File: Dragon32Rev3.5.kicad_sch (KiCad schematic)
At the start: 8 parts, among them SW1 RESET

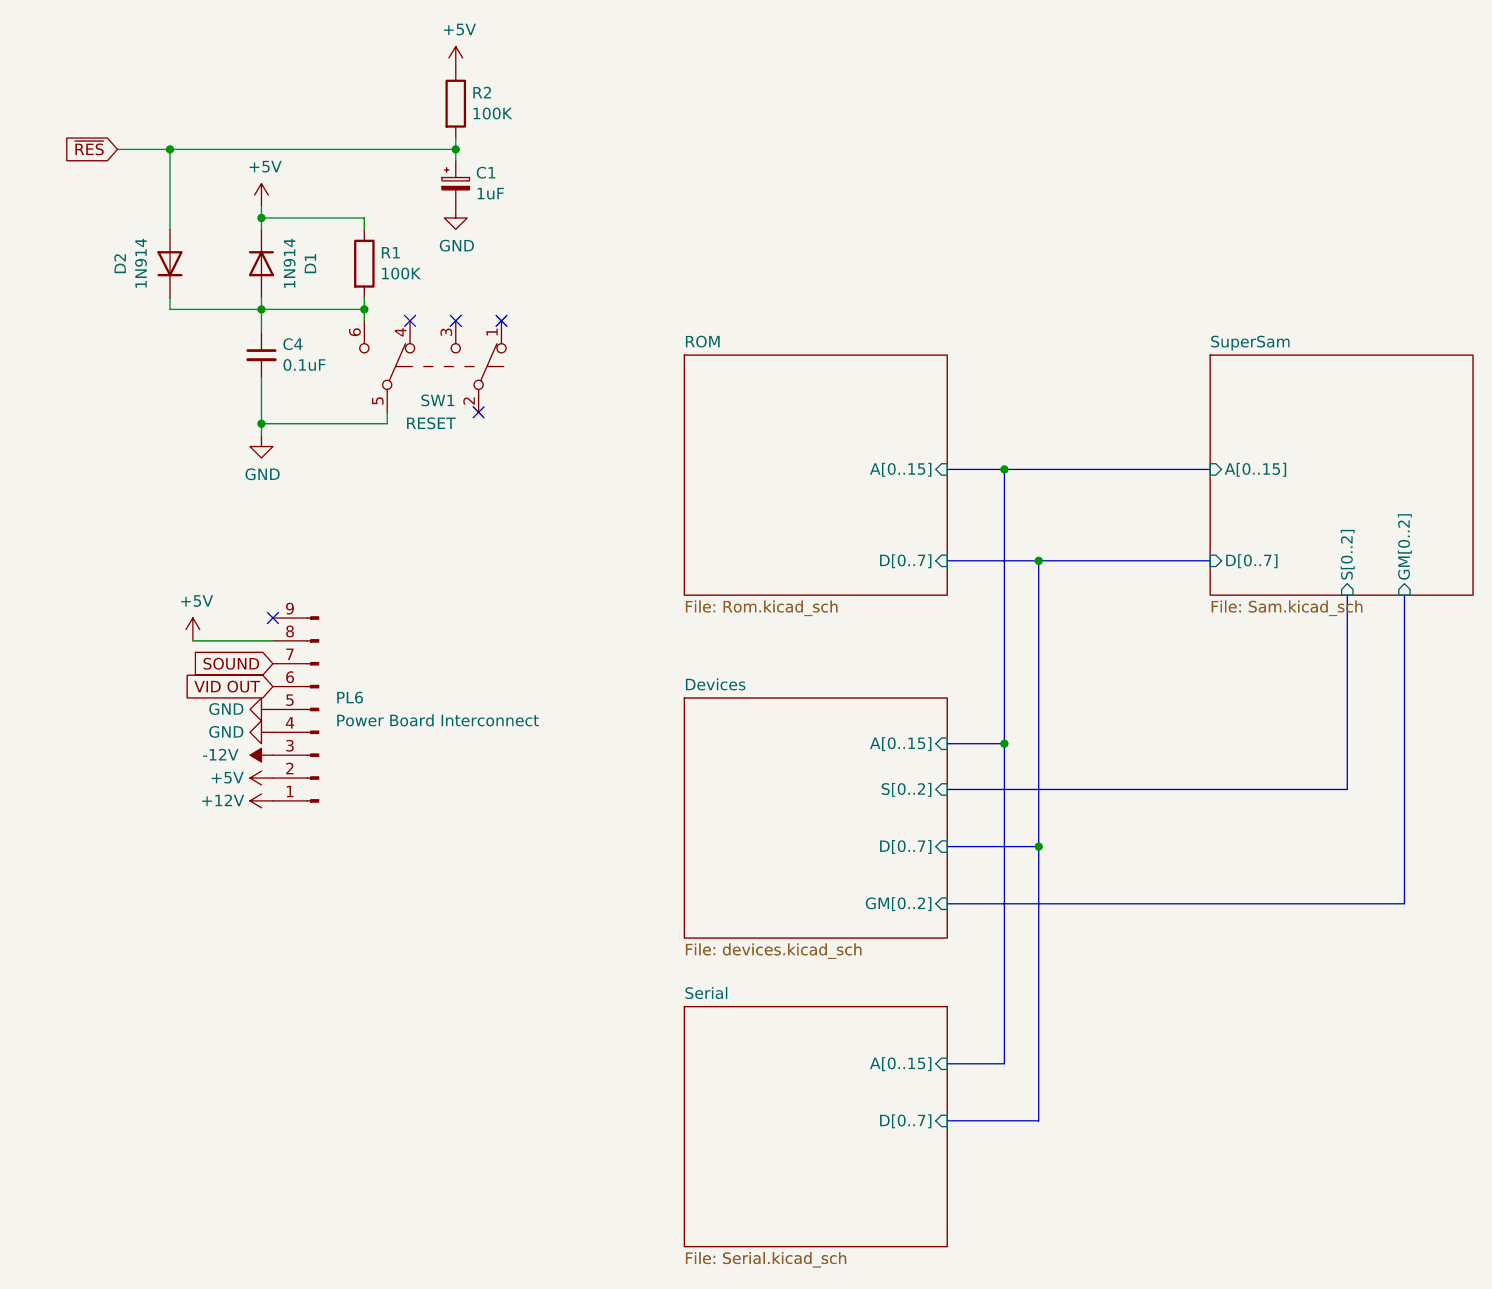
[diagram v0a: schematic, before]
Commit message: add audio support
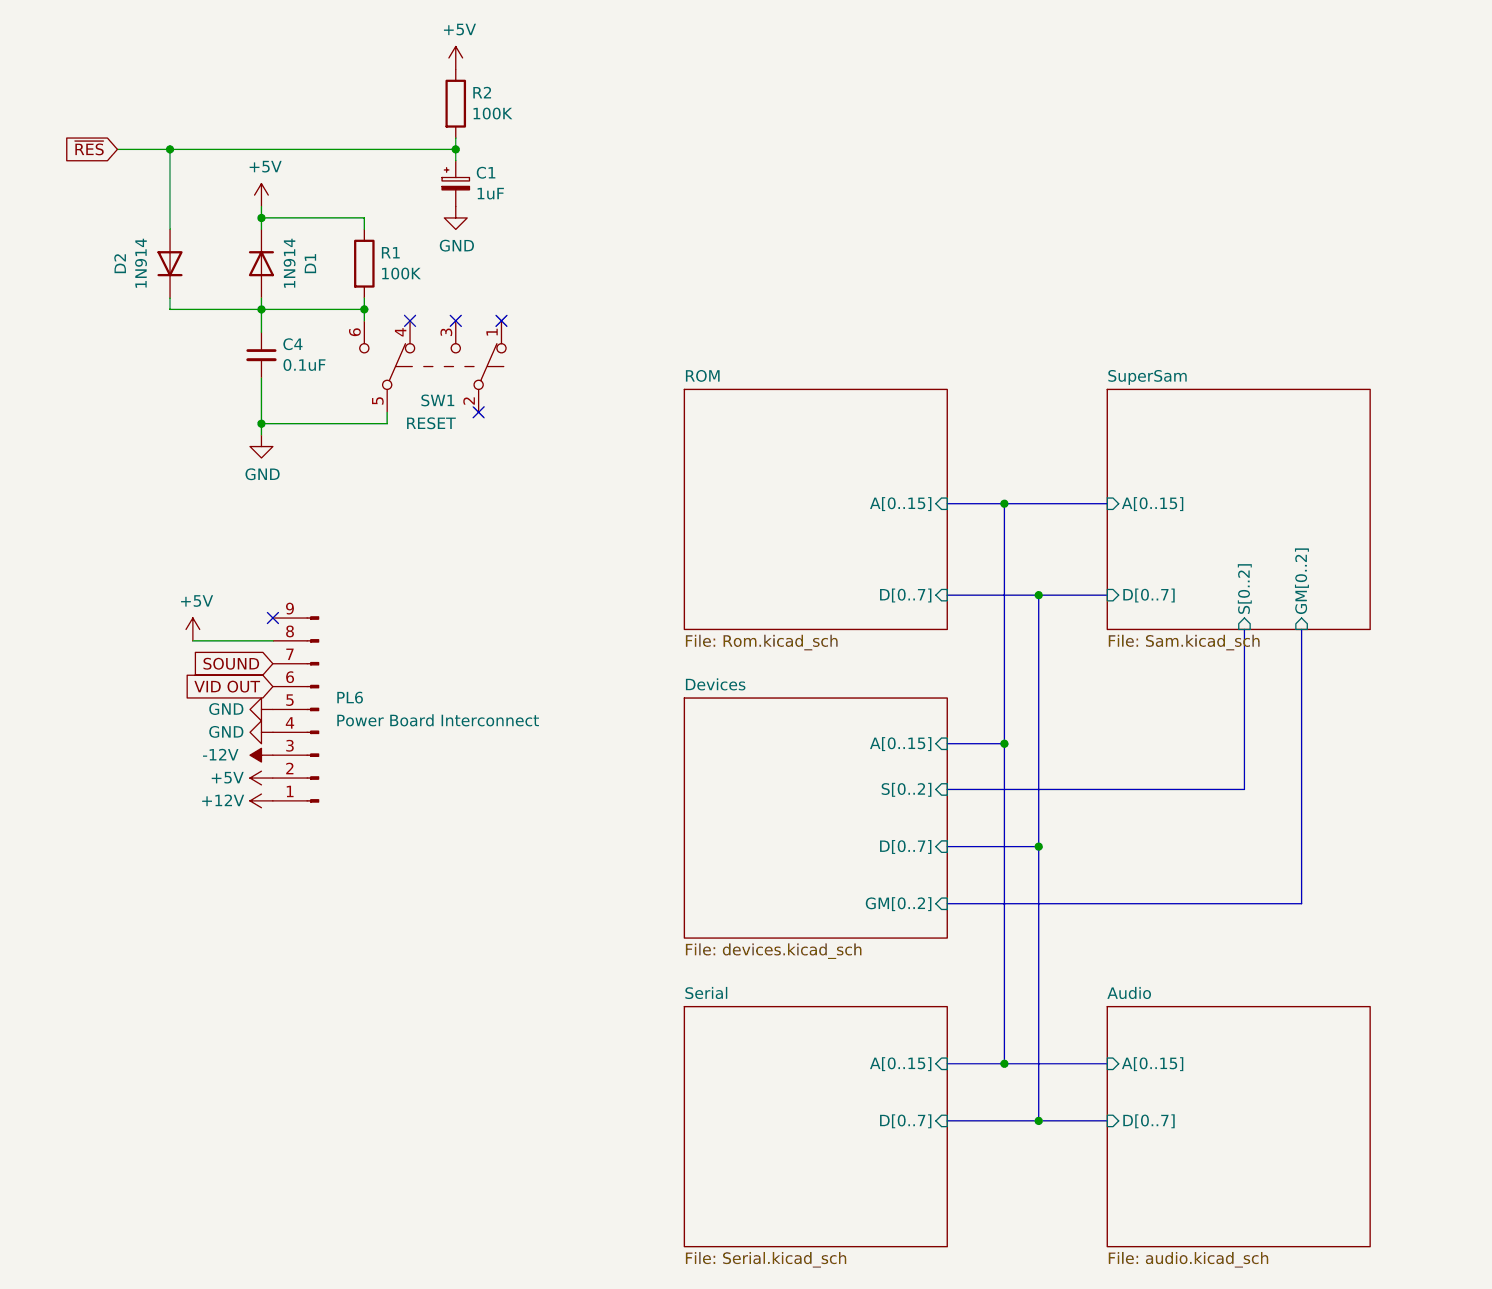
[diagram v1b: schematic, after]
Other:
- added sheet Audio (audio.kicad_sch)
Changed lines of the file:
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@@
 	)
 	(junction
-		(at 119.38 64.77)
+		(at 119.38 130.81)
+		(diameter 0)
+		(color 0 0 0 0)
+	)
+	(junction
+		(at 119.38 68.58)
+		(diameter 0)
+		(color 0 0 0 0)
+	)
+	(junction
+		(at 123.19 137.16)
 		(diameter 0)
 		(color 0 0 0 0)
@@
 	)
 	(junction
-		(at 123.19 74.93)
+		(at 123.19 78.74)
 		(diameter 0)
 		(color 0 0 0 0)
@@
 	(bus
 		(pts
-			(xy 123.19 106.68) (xy 123.19 74.93)
+			(xy 123.19 137.16) (xy 130.81 137.16)
 		)
 		(stroke
@@
 	(bus
 		(pts
-			(xy 119.38 64.77) (xy 142.24 64.77)
+			(xy 123.19 106.68) (xy 123.19 78.74)
+		)
+		(stroke
+			(width 0)
+			(type default)
+		)
+	)
+	(bus
+		(pts
+			(xy 119.38 68.58) (xy 130.81 68.58)
 		)
 		(stroke
@@
 	(bus
 		(pts
-			(xy 123.19 74.93) (xy 142.24 74.93)
+			(xy 123.19 78.74) (xy 130.81 78.74)
 		)
 		(stroke
@@
 	(bus
 		(pts
-			(xy 113.03 74.93) (xy 123.19 74.93)
+			(xy 113.03 78.74) (xy 123.19 78.74)
 		)
 		(stroke
@@
 	(bus
 		(pts
-			(xy 113.03 113.03) (xy 163.83 113.03)
+			(xy 113.03 113.03) (xy 152.4 113.03)
 		)
 		(stroke
@@
 	(bus
 		(pts
-			(xy 157.48 78.74) (xy 157.48 100.33)
+			(xy 146.05 82.55) (xy 146.05 100.33)
 		)
 		(stroke
@@
 	(bus
 		(pts
-			(xy 119.38 95.25) (xy 119.38 64.77)
+			(xy 119.38 95.25) (xy 119.38 68.58)
 		)
 		(stroke
@@
 	(bus
 		(pts
-			(xy 157.48 100.33) (xy 113.03 100.33)
+			(xy 146.05 100.33) (xy 113.03 100.33)
 		)
 		(stroke
@@
 	(bus
 		(pts
-			(xy 113.03 64.77) (xy 119.38 64.77)
+			(xy 113.03 68.58) (xy 119.38 68.58)
 		)
 		(stroke
@@
 		)
 	)
+	(bus
+		(pts
+			(xy 119.38 130.81) (xy 130.81 130.81)
+		)
+		(stroke
+			(width 0)
+			(type default)
+		)
+	)
 	(wire
 		(pts
@@
 	(bus
 		(pts
-			(xy 163.83 113.03) (xy 163.83 78.74)
+			(xy 152.4 113.03) (xy 152.4 82.55)
 		)
 		(stroke
@@
 	)
 	(sheet
-		(at 142.24 52.07)
+		(at 130.81 55.88)
 		(size 29.21 26.67)
 		(exclude_from_sim no)
@@
 		)
 		(property "Sheetname" "SuperSam"
-			(at 142.24 51.3584 0)
+			(at 130.81 55.1684 0)
 			(effects
 				(font
@@
 		)
 		(property "Sheetfile" "Sam.kicad_sch"
-			(at 142.24 79.3246 0)
+			(at 130.81 83.1346 0)
 			(effects
 				(font
@@
 		)
 		(pin "S[0..2]" input
-			(at 157.48 78.74 270)
+			(at 146.05 82.55 270)
 			(effects
 				(font
@@
 		)
 		(pin "D[0..7]" input
-			(at 142.24 74.93 180)
+			(at 130.81 78.74 180)
 			(effects
 				(font
@@
 		)
 		(pin "GM[0..2]" input
-			(at 163.83 78.74 270)
+			(at 152.4 82.55 270)
 			(effects
 				(font
@@
 		)
 		(pin "A[0..15]" input
-			(at 142.24 64.77 180)
+			(at 130.81 68.58 180)
 			(effects
 				(font
@@
 				(path "/07816fd1-49cc-44df-9615-6cd7402e0f24"
 					(page "2")
+				)
+			)
+		)
+	)
+	(sheet
+		(at 130.81 124.46)
+		(size 29.21 26.67)
+		(exclude_from_sim no)
+		(in_bom yes)
+		(on_board yes)
+		(dnp no)
+		(fields_autoplaced yes)
+		(stroke
+			(width 0.1524)
+			(type solid)
+		)
+		(fill
+			(color 0 0 0 0.0000)
+		)
+		(property "Sheetname" "Audio"
+			(at 130.81 123.7484 0)
+			(effects
+				(font
+					(size 1.27 1.27)
+				)
+				(justify left bottom)
+			)
+		)
+		(property "Sheetfile" "audio.kicad_sch"
+			(at 130.81 151.7146 0)
+			(effects
+				(font
+					(size 1.27 1.27)
+				)
+				(justify left top)
+			)
+		)
+		(pin "A[0..15]" input
+			(at 130.81 130.81 180)
+			(effects
+				(font
+					(size 1.27 1.27)
+				)
+				(justify left)
+			)
+		)
+		(pin "D[0..7]" input
+			(at 130.81 137.16 180)
+			(effects
+				(font
+					(size 1.27 1.27)
+				)
+				(justify left)
+			)
+		)
+		(instances
+			(project "Dragon32Rev3.5"
+				(path "/07816fd1-49cc-44df-9615-6cd7402e0f24"
+					(page "7")
 				)
 			)
@@
 	)
 	(sheet
-		(at 83.82 52.07)
+		(at 83.82 55.88)
 		(size 29.21 26.67)
 		(exclude_from_sim no)
@@
 		)
 		(property "Sheetname" "ROM"
-			(at 83.82 51.3584 0)
+			(at 83.82 55.1684 0)
 			(effects
 				(font
@@
 		)
 		(property "Sheetfile" "Rom.kicad_sch"
-			(at 83.82 79.3246 0)
+			(at 83.82 83.1346 0)
 			(effects
 				(font
@@
 		)
 		(pin "D[0..7]" input
-			(at 113.03 74.93 0)
+			(at 113.03 78.74 0)
 			(effects
 				(font
@@
 		)
 		(pin "A[0..15]" input
-			(at 113.03 64.77 0)
-			(effects
-				(font
+			(at 113.03 68.58 0)
+			(effects
+				(font
